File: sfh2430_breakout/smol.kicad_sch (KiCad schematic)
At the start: 3 parts, among them J6 Conn_01x01, J7 Conn_01x01

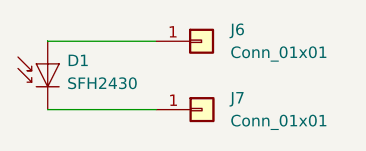
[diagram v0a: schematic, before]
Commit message: add math and decals
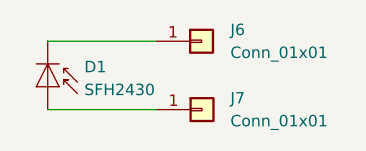
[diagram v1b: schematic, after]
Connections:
- net at J7.1 (Pin_1): now also D1.2 (A); no longer D1.1 (K)
- net at J6.1 (Pin_1): now also D1.1 (K); no longer D1.2 (A)
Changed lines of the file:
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@@
     )
   )
-  (symbol (lib_id "Sensor_Optical:SFH2430") (at 153.6954 86.8172 90) (unit 1)
+  (symbol (lib_id "Sensor_Optical:SFH2430") (at 153.6954 89.3572 270) (unit 1)
     (in_bom yes) (on_board yes) (dnp no) (fields_autoplaced)
-    (property "Reference" "D1" (at 155.8544 86.4743 90)
-      (effects (font (size 1.27 1.27)) (justify right))
+    (property "Reference" "D1" (at 157.7594 87.1601 90)
+      (effects (font (size 1.27 1.27)) (justify left))
     )
-    (property "Value" "SFH2430" (at 155.8544 89.0143 90)
-      (effects (font (size 1.27 1.27)) (justify right))
+    (property "Value" "SFH2430" (at 157.7594 89.7001 90)
+      (effects (font (size 1.27 1.27)) (justify left))
     )
-    (property "Footprint" "OptoDevice:Osram_SFH2430" (at 149.2504 86.8172 0)
+    (property "Footprint" "OptoDevice:Osram_SFH2430" (at 158.1404 89.3572 0)
       (effects (font (size 1.27 1.27)) hide)
     )

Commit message: ordered sfh2430 breakout rev 0.1
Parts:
- D1: footprint OptoDevice:Osram_SFH2430 -> adcs:Osram_SFH2430
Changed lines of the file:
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@@
       (effects (font (size 1.27 1.27)) (justify left))
     )
-    (property "Footprint" "OptoDevice:Osram_SFH2430" (at 158.1404 89.3572 0)
+    (property "Footprint" "adcs:Osram_SFH2430" (at 158.1404 89.3572 0)
       (effects (font (size 1.27 1.27)) hide)
     )
@@
       (effects (font (size 1.27 1.27)) hide)
     )
+    (property "DigiKey Part Number" "" (at 153.6954 89.3572 0)
+      (effects (font (size 1.27 1.27)) hide)
+    )
+    (property "Tolerance" "" (at 153.6954 89.3572 0)
+      (effects (font (size 1.27 1.27)))
+    )
+    (property "Power Rating" "" (at 153.6954 89.3572 0)
+      (effects (font (size 1.27 1.27)))
+    )
     (pin "1")

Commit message: sfh2400 v2 (flex PCB)
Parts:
- removed D1: SFH2430, adcs:Osram_SFH2430, symbol Sensor_Optical:SFH2430
- removed J6, J7: Conn_01x01, adcs:castellated_05mm, symbol Connector_Generic:Conn_01x01
- added C?: 100nF, Capacitor_SMD:C_0603_1608Metric, symbol mainboard:22UF-1210-16V-20%
- added C?: 1nF, Capacitor_SMD:C_0603_1608Metric, symbol mainboard:22UF-1210-16V-20%
- added D?: SFH2430, adcs:Osram_SFH2430, symbol Sensor_Optical:SFH2430
- added R?: 3.9k, Resistor_SMD:R_0603_1608Metric, symbol pycubed_mainboard:RESISTOR0603
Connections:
- new net IN+: D?.2 (A)
- new net IN-: C?.1, C?.1, D?.1 (K), R?.1
- new net OUT: C?.2, C?.2, R?.2
